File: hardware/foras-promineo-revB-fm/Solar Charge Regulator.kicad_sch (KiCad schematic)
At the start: 21 parts, among them U211 ‎LT3652HVEMSE#TRPBF‎

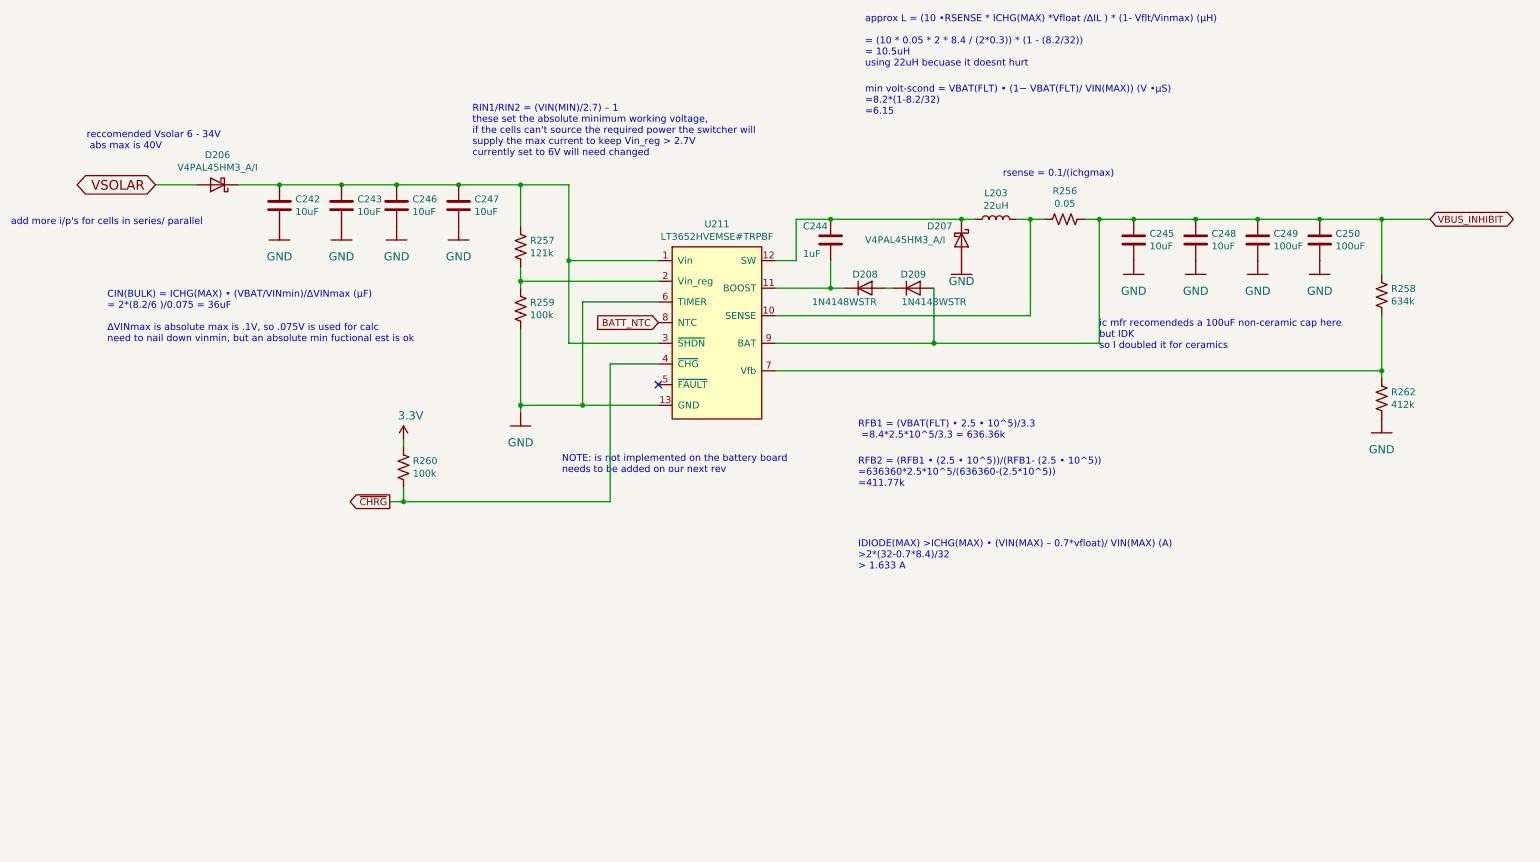
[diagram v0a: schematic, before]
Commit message: added charge current monitor
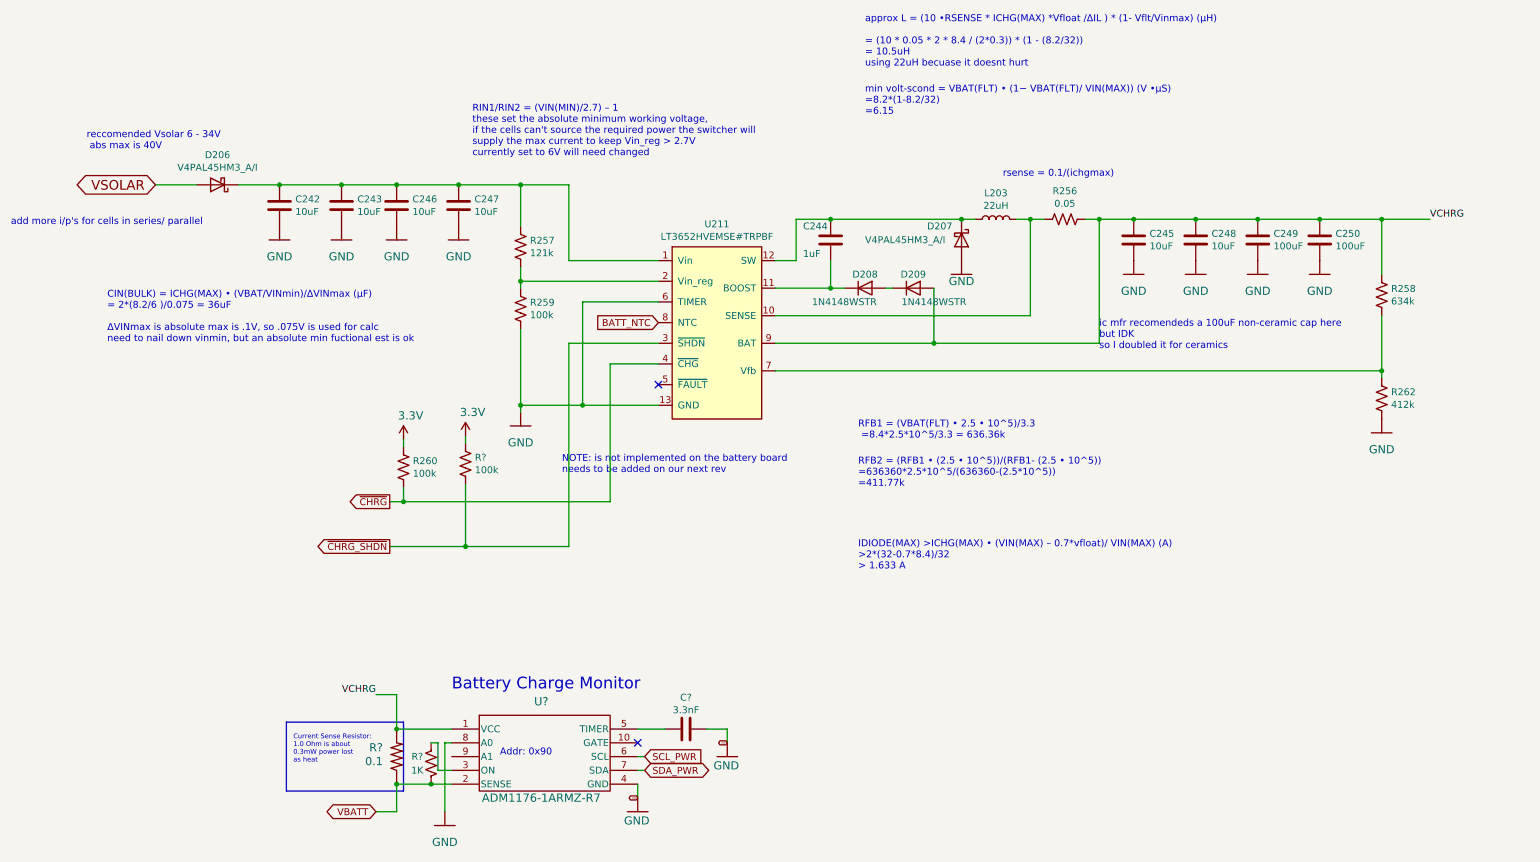
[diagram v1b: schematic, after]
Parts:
- added C?: 3.3nF, Capacitor_SMD:C_0603_1608Metric, symbol mainboard-rescue:C-Device-mainboard-rescue
- added R?: 1K, Resistor_SMD:R_0603_1608Metric, symbol mainboard-rescue:R_US-Device-mainboard-rescue
- added R?: 0.1, Resistor_SMD:R_2512_6332Metric, symbol mainboard:R-US_R2512
- added R?: 100k, Resistor_SMD:R_0603_1608Metric, symbol mainboard-rescue:R_US-Device-mainboard-rescue
- added U?: ADM1176-1ARMZ-R7, mainboard:ADM1176-1ARMZ-R7, symbol mainboard:ADM1176-1ARMZ-R7
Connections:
- net 3.3V: now also R?.1
- net GND: now also C?.1, U?.4 (GND), U?.8 (A0)
- net at C242.1, C243.1, C246.1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: no longer U211.3 (~{SHDN})
- net VBUS_INHIBIT renamed VCHRG
- net VCHRG: now also R?.2, U?.1 (VCC)
- new net: R?.2, U?.3 (ON)
- new net: C?.2, U?.5 (TIMER)
- new net SCL_PWR: U?.6 (SCL)
- new net SDA_PWR: U?.7 (SDA)
- new net VBATT: R?.1, R?.1, U?.2 (SENSE)
- new net ~{CHRG_SHDN}: R?.2, U211.3 (~{SHDN})
- no-connect marks 1 -> 2
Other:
- note added: "Addr: 0x90"
- note added: "Battery Charge Monitor"
- note added: "Current Sense Resistor: 1.0 Ohm is about 0.3mW power lost as heat"

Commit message: friday updates
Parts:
- gave numbers to parts that had none: 5
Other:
- note added: "current TO batt"
- note added: "implement mppt with solar telem's"
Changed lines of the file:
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@@
     (stroke (width 0) (type default) (color 0 0 0 0))
   )
-  (text "Battery Charge Monitor" (at 82.55 155.575 0)
+  (text "Battery Charge Monitor" (at 82.55 153.67 0)
     (effects (font (size 2.159 2.159)) (justify left bottom))
   )
@@
     (effects (font (size 1.27 1.27)) (justify left bottom))
   )
+  (text "current TO batt" (at 82.55 156.21 0)
+    (effects (font (size 1.27 1.27)) (justify left bottom))
+  )
   (text "CIN(BULK) = ICHG(MAX) • (VBAT/VINmin)/ΔVINmax (µF) \n= 2*(8.2/6 )/0.075 = 36uF\n\nΔVINmax is absolute max is .1V, so .075V is used for calc\nneed to nail down vinmin, but an absolute min fuctional est is ok"
     (at 19.05 91.44 0)
@@
   (text "add more i/p's for cells in series/ parallel" (at 1.27 69.85 0)
     (effects (font (size 1.27 1.27)) (justify left bottom))
+  )
+  (text "implement mppt with solar telem's" (at 19.05 96.52 0)
+    (effects (font (size 1.27 1.27) (thickness 0.254) bold) (justify left bottom))
   )
   (text "rsense = 0.1/(ichgmax)" (at 184.15 60.96 0)
@@
     (effects (font (size 1.27 1.27)) (justify left bottom))
   )
-  (label "VCHRG" (at 262.89 68.58 0)
-    (effects (font (size 1.27 1.27)) (justify left bottom))
-  )
-  (label "VCHRG" (at 68.58 156.21 180)
-    (effects (font (size 1.27 1.27)) (justify right bottom))
+  (global_label "VCHRG" (shape input) (at 262.89 68.58 0) (fields_autoplaced)
+    (effects (font (size 1.27 1.27)) (justify left))
+    (property "Intersheet References" "${INTERSHEET_REFS}" (id 0) (at 271.4432 68.5006 0)
+      (effects (font (size 1.27 1.27)) (justify left) hide)
+    )
   )
   (global_label "~{CHRG}" (shape output) (at 71.12 120.65 180) (fields_autoplaced)
@@
     (property "Intersheet References" "${INTERSHEET_REFS}" (id 0) (at -46.99 67.31 0)
       (effects (font (size 1.27 1.27)) hide)
+    )
+  )
+  (global_label "VCHRG" (shape input) (at 68.58 156.21 180) (fields_autoplaced)
+    (effects (font (size 1.27 1.27)) (justify right))
+    (property "Intersheet References" "${INTERSHEET_REFS}" (id 0) (at 60.0268 156.2894 0)
+      (effects (font (size 1.27 1.27)) (justify right) hide)
     )
   )
@@
   (symbol (lib_id "mainboard:GND") (at 116.84 177.8 0) (unit 1)
     (in_bom yes) (on_board yes)
-    (property "Reference" "#GND?" (id 0) (at 116.84 177.8 0)
+    (property "Reference" "#GND0113" (id 0) (at 116.84 177.8 0)
       (effects (font (size 1.27 1.27)) hide)
     )
@@
   (symbol (lib_id "mainboard:3.3V") (at 85.09 108.585 0) (unit 1)
     (in_bom yes) (on_board yes)
-    (property "Reference" "#P+?" (id 0) (at 85.09 108.585 0)
+    (property "Reference" "#P+0103" (id 0) (at 85.09 108.585 0)
       (effects (font (size 1.27 1.27)) hide)
     )
@@
   (symbol (lib_id "mainboard-rescue:R_US-Device-mainboard-rescue") (at 78.74 168.91 0) (mirror x) (unit 1)
     (in_bom yes) (on_board yes)
-    (property "Reference" "R?" (id 0) (at 76.2 167.64 0))
+    (property "Reference" "R18" (id 0) (at 76.2 167.64 0))
     (property "Value" "1K" (id 1) (at 76.2 170.18 0))
     (property "Footprint" "Resistor_SMD:R_0603_1608Metric" (id 2) (at 79.756 168.656 90)
@@
   (symbol (lib_id "mainboard:GND") (at 81.28 180.34 0) (unit 1)
     (in_bom yes) (on_board yes)
-    (property "Reference" "#GND?" (id 0) (at 81.28 180.34 0)
+    (property "Reference" "#GND0112" (id 0) (at 81.28 180.34 0)
       (effects (font (size 1.27 1.27)) hide)
     )
@@
   (symbol (lib_id "mainboard:GND") (at 133.35 167.64 0) (unit 1)
     (in_bom yes) (on_board yes)
-    (property "Reference" "#GND?" (id 0) (at 133.35 167.64 0)
+    (property "Reference" "#GND0111" (id 0) (at 133.35 167.64 0)
       (effects (font (size 1.27 1.27)) hide)
     )
@@
   (symbol (lib_id "mainboard:ADM1176-1ARMZ-R7") (at 80.01 148.59 0) (unit 1)
     (in_bom yes) (on_board yes)
-    (property "Reference" "U?" (id 0) (at 99.06 157.48 0)
+    (property "Reference" "U3" (id 0) (at 99.06 157.48 0)
       (effects (font (size 1.524 1.524)))
     )
@@
   (symbol (lib_id "mainboard-rescue:C-Device-mainboard-rescue") (at 125.73 162.56 270) (unit 1)
     (in_bom yes) (on_board yes)
-    (property "Reference" "C?" (id 0) (at 125.73 156.7434 90))
+    (property "Reference" "C7" (id 0) (at 125.73 156.7434 90))
     (property "Value" "3.3nF" (id 1) (at 125.73 159.0548 90))
     (property "Footprint" "Capacitor_SMD:C_0603_1608Metric" (id 2) (at 125.73 162.56 0)
@@
   (symbol (lib_id "mainboard:R-US_R2512") (at 72.39 167.64 90) (unit 1)
     (in_bom yes) (on_board yes)
-    (property "Reference" "R?" (id 0) (at 69.85 165.1 90)
+    (property "Reference" "R17" (id 0) (at 69.85 165.1 90)
       (effects (font (size 1.4986 1.4986)) (justify left bottom))
     )
@@
   (symbol (lib_id "mainboard-rescue:R_US-Device-mainboard-rescue") (at 85.09 113.665 0) (unit 1)
     (in_bom yes) (on_board yes)
-    (property "Reference" "R?" (id 0) (at 86.8172 112.4966 0)
-      (effects (font (size 1.27 1.27)) (justify left))
-    )
+    (property "Reference" "R19" (id 0) (at 86.8172 112.4966 0)
+      (effects (font (size 1.27 1.27)) (justify left))
+    )

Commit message: text changes
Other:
- note added: "SUB L203 for 7447709220!!!!"
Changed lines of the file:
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@@
     (effects (font (size 1.27 1.27)) (justify left bottom))
+  )
+  (text "SUB L203 for 7447709220!!!!" (at 125.73 146.05 0)
+    (effects (font (size 2 2) (thickness 0.4) bold) (justify left bottom))
   )
   (text "current TO batt" (at 82.55 156.21 0)

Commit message: fm sch changes
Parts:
- removed C249, C250: 100uF, Capacitor_SMD:C_1210_3225Metric, symbol mainboard-rescue:C-Device-mainboard-rescue
- added C51: 100uF, symbol Device:C_Polarized_US
- added R116: 10k, Resistor_SMD:R_0603_1608Metric, symbol Device:R_US
- added TH53: 10k, Resistor_SMD:R_0603_1608Metric, symbol Device:Thermistor_NTC_US
- C242, C243, C244, C245, C246, C247, C248, C7: symbol mainboard-rescue:C-Device-mainboard-rescue -> Device:C
- L203: footprint Inductor_SMD:L_Vishay_IHLP-2525 -> (none); symbol mainboard-rescue:L-Device-mainboard-rescue -> Device:L
- R17: symbol mainboard:R-US_R2512 -> Device:R_US
- R18: value 1K -> 1k; symbol mainboard-rescue:R_US-Device-mainboard-rescue -> Device:R_US
- R19, R256, R257, R258, R259, R260, R262: symbol mainboard-rescue:R_US-Device-mainboard-rescue -> Device:R_US
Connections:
- net 3.3V: now also R116.1
- net GND: now also C51.2, TH53.2
- net VBATT: no longer R17.1
- net VCHRG: now also C51.1; no longer R17.2
- new net SLR_CHRG_NTC: R116.2, TH53.1
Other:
- note removed: "NOTE: is not implemented on the battery board needs to be added on our next rev"

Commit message: fm layout work
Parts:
- removed D209: 1N4148WSTR, Diode_SMD:D_SOD-323, symbol mainboard-rescue:D-Device-mainboard-rescue
- added R133: 412k, Resistor_SMD:R_0603_1608Metric, symbol Device:R_US
- C51: footprint (none) -> Capacitor_Tantalum_SMD:CP_EIA-7343-43_Kemet-X
- L203: footprint (none) -> Inductor_SMD:L_Wuerth_WE-PD-Typ-LS
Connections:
- net VBATT: now also R17.1
- net VCHRG: now also D208.2 (A), R17.2
- net at R258.2, R262.1: now also R133.2; no longer U211.7 (Vfb)
- new net: R133.1, U211.7 (Vfb)
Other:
- moved on the sheet: R17, R262
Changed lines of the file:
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@@
   (junction (at 73.66 120.65) (diameter 0) (color 0 0 0 0)
   )
+  (junction (at 72.39 172.72) (diameter 0) (color 0 0 0 0)
+  )
   (junction (at 95.25 80.01) (diameter 0) (color 0 0 0 0)
   )
@@
   )
   (junction (at 106.68 102.87) (diameter 0) (color 0 0 0 0)
+  )
+  (junction (at 72.39 162.56) (diameter 0) (color 0 0 0 0)
   )
   (junction (at 176.53 68.58) (diameter 0) (color 0 0 0 0)
@@
   (no_connect (at 116.84 165.1))
   (no_connect (at 120.65 99.06))
-  (wire (pts (xy 163.83 81.28) (xy 162.56 81.28))
+  (wire (pts (xy 162.56 81.28) (xy 171.45 81.28))
     (stroke (width 0) (type default) (color 0 0 0 0))
   )
@@
     (stroke (width 0) (type default) (color 0 0 0 0))
   )
+  (wire (pts (xy 72.39 171.45) (xy 72.39 172.72))
+    (stroke (width 0) (type default) (color 0 0 0 0))
+  )
   (wire (pts (xy 118.11 170.18) (xy 116.84 170.18))
     (stroke (width 0) (type default) (color 0 0 0 0))
@@
     (stroke (width 0) (type default) (color 0 0 0 0))
   )
-  (wire (pts (xy 142.24 96.52) (xy 254 96.52))
-    (stroke (width 0) (type default) (color 0 0 0 0))
-  )
-  (polyline (pts (xy 73.66 161.29) (xy 73.66 173.99))
+  (wire (pts (xy 142.24 96.52) (xy 240.03 96.52))
+    (stroke (width 0) (type default) (color 0 0 0 0))
+  )
+  (polyline (pts (xy 72.39 161.29) (xy 72.39 173.99))
     (stroke (width 0) (type default) (color 0 0 0 0))
   )
@@
     (stroke (width 0) (type default) (color 0 0 0 0))
   )
-  (polyline (pts (xy 73.66 173.99) (xy 52.07 173.99))
+  (polyline (pts (xy 72.39 173.99) (xy 52.07 173.99))
     (stroke (width 0) (type default) (color 0 0 0 0))
   )
@@
     (stroke (width 0) (type default) (color 0 0 0 0))
   )
-  (polyline (pts (xy 52.07 161.29) (xy 73.66 161.29))
+  (polyline (pts (xy 52.07 161.29) (xy 72.39 161.29))
     (stroke (width 0) (type default) (color 0 0 0 0))
   )
@@
     (stroke (width 0) (type default) (color 0 0 0 0))
   )
+  (wire (pts (xy 72.39 162.56) (xy 72.39 163.83))
+    (stroke (width 0) (type default) (color 0 0 0 0))
+  )
   (wire (pts (xy 72.39 162.56) (xy 72.39 156.21))
     (stroke (width 0) (type default) (color 0 0 0 0))
@@
     (stroke (width 0) (type default) (color 0 0 0 0))
   )
+  (wire (pts (xy 247.65 96.52) (xy 254 96.52))
+    (stroke (width 0) (type default) (color 0 0 0 0))
+  )
   (wire (pts (xy 106.68 102.87) (xy 95.25 102.87))
     (stroke (width 0) (type default) (color 0 0 0 0))
@@
     (stroke (width 0) (type default) (color 0 0 0 0))
   )
-  (wire (pts (xy 254 96.52) (xy 254 97.79))
+  (wire (pts (xy 254 96.52) (xy 254 102.87))
     (stroke (width 0) (type default) (color 0 0 0 0))
   )
@@
     (property "Reference" "L203" (id 0) (at 182.88 63.754 90))
     (property "Value" "22uH" (id 1) (at 182.88 66.0654 90))
-    (property "Footprint" "" (id 2) (at 182.88 68.58 0)
+    (property "Footprint" "Inductor_SMD:L_Wuerth_WE-PD-Typ-LS" (id 2) (at 182.88 68.58 0)
       (effects (font (size 1.27 1.27)) hide)
     )
@@
     (pin "2")
   )
-  (symbol (lib_id "Device:R_US") (at 254 101.6 0) (unit 1)
-    (in_bom yes) (on_board yes)
-    (property "Reference" "R262" (id 0) (at 255.7272 100.4316 0)
-      (effects (font (size 1.27 1.27)) (justify left))
-    )
-    (property "Value" "412k" (id 1) (at 255.7272 102.743 0)
-      (effects (font (size 1.27 1.27)) (justify left))
-    )
-    (property "Footprint" "Resistor_SMD:R_0603_1608Metric" (id 2) (at 255.016 101.854 90)
-      (effects (font (size 1.27 1.27)) hide)
-    )
-    (property "Datasheet" "~" (id 3) (at 254 101.6 0)
-      (effects (font (size 1.27 1.27)) hide)
-    )
-    (pin "1")
-    (pin "2")
-  )
-  (symbol (lib_id "mainboard:GND") (at 254 107.95 0) (unit 1)
-    (in_bom yes) (on_board yes)
-    (property "Reference" "#GND0209" (id 0) (at 254 107.95 0)
-      (effects (font (size 1.27 1.27)) hide)
-    )
-    (property "Value" "GND" (id 1) (at 254 111.0234 0)
+  (symbol (lib_id "Device:R_US") (at 254 106.68 0) (unit 1)
+    (in_bom yes) (on_board yes)
+    (property "Reference" "R262" (id 0) (at 255.7272 105.5116 0)
+      (effects (font (size 1.27 1.27)) (justify left))
+    )
+    (property "Value" "412k" (id 1) (at 255.7272 107.823 0)
+      (effects (font (size 1.27 1.27)) (justify left))
+    )
+    (property "Footprint" "Resistor_SMD:R_0603_1608Metric" (id 2) (at 255.016 106.934 90)
+      (effects (font (size 1.27 1.27)) hide)
+    )
+    (property "Datasheet" "~" (id 3) (at 254 106.68 0)
+      (effects (font (size 1.27 1.27)) hide)
+    )
+    (pin "1")
+    (pin "2")
+  )
+  (symbol (lib_id "mainboard:GND") (at 254 113.03 0) (unit 1)
+    (in_bom yes) (on_board yes)
+    (property "Reference" "#GND0209" (id 0) (at 254 113.03 0)
+      (effects (font (size 1.27 1.27)) hide)
+    )
+    (property "Value" "GND" (id 1) (at 254 116.1034 0)
       (effects (font (size 1.4986 1.4986)))
     )
-    (property "Footprint" "" (id 2) (at 254 107.95 0)
-      (effects (font (size 1.27 1.27)) hide)
-    )
-    (property "Datasheet" "" (id 3) (at 254 107.95 0)
+    (property "Footprint" "" (id 2) (at 254 113.03 0)
+      (effects (font (size 1.27 1.27)) hide)
+    )
+    (property "Datasheet" "" (id 3) (at 254 113.03 0)
       (effects (font (size 1.27 1.27)) hide)
     )
@@
     )
     (pin "1")
-  )
-  (symbol (lib_id "mainboard-rescue:D-Device-mainboard-rescue") (at 167.64 81.28 0) (unit 1)
-    (in_bom yes) (on_board yes)
-    (property "Reference" "D209" (id 0) (at 167.64 78.74 0))
-    (property "Value" "1N4148WSTR" (id 1) (at 171.45 83.82 0))
-    (property "Footprint" "Diode_SMD:D_SOD-323" (id 2) (at 167.64 81.28 0)
-      (effects (font (size 1.27 1.27)) hide)
-    )
-    (property "Datasheet" "~" (id 3) (at 167.64 81.28 0)
-      (effects (font (size 1.27 1.27)) hide)
-    )
-    (pin "1")
-    (pin "2")
   )
   (symbol (lib_id "mainboard-rescue:D-Device-mainboard-rescue") (at 158.75 81.28 0) (unit 1)
@@
       (effects (font (size 1.27 1.27)) (justify left))
     )
-    (property "Footprint" "" (id 2) (at 233.68 72.39 0)
-      (effects (font (size 1.27 1.27)) hide)
-    )
-    (property "Datasheet" "~" (id 3) (at 233.68 72.39 0)
+    (property "Footprint" "Capacitor_Tantalum_SMD:CP_EIA-7343-43_Kemet-X" (id 2) (at 233.68 72.39 0)
+      (effects (font (size 1.27 1.27)) hide)
+    )
+    (property "Datasheet" "T498X107K016ATE075" (id 3) (at 233.68 72.39 0)
       (effects (font (size 1.27 1.27)) hide)
     )
@@
     )
     (pin "1")
+  )
+  (symbol (lib_id "Device:R_US") (at 243.84 96.52 90) (unit 1)
+    (in_bom yes) (on_board yes)
+    (property "Reference" "R133" (id 0) (at 242.6716 94.7928 0)
+      (effects (font (size 1.27 1.27)) (justify left))
+    )
+    (property "Value" "412k" (id 1) (at 244.983 94.7928 0)
+      (effects (font (size 1.27 1.27)) (justify left))
+    )
+    (property "Footprint" "Resistor_SMD:R_0603_1608Metric" (id 2) (at 244.094 95.504 90)
+      (effects (font (size 1.27 1.27)) hide)
+    )
+    (property "Datasheet" "~" (id 3) (at 243.84 96.52 0)
+      (effects (font (size 1.27 1.27)) hide)
+    )
+    (pin "1")
+    (pin "2")
   )
   (symbol (lib_id "Device:Thermistor_NTC_US") (at 30.48 146.05 0) (unit 1)
@@
     (pin "2")
   )
-  (symbol (lib_id "Device:R_US") (at 72.39 167.64 90) (unit 1)
-    (in_bom yes) (on_board yes)
-    (property "Reference" "R17" (id 0) (at 69.85 165.1 90)
+  (symbol (lib_id "Device:R_US") (at 72.39 167.64 180) (unit 1)
+    (in_bom yes) (on_board yes)
+    (property "Reference" "R17" (id 0) (at 71.12 165.1 0)
       (effects (font (size 1.4986 1.4986)) (justify left bottom))
     )
-    (property "Value" "0.1" (id 1) (at 69.85 167.64 90)
+    (property "Value" "0.1" (id 1) (at 71.12 167.64 0)
       (effects (font (size 1.4986 1.4986)) (justify left bottom))
     )
@@
       (effects (font (size 1.27 1.27)) hide)
     )
-    (property "Description" "" (id 4) (at 67.31 165.1 0)
-      (effects (font (size 1.27 1.27)) hide)
-    )
+    (property "Description" "" (id 4) (at 69.85 172.72 0)
+      (effects (font (size 1.27 1.27)) hide)
+    )
